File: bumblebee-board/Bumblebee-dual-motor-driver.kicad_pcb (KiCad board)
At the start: 2 copper layers, 91.8 x 75.9 mm, 94 parts, among them J1 ICSP, J10 GND, J11 MOTOR1_A, J12 MOTOR1_B, J13 MOTOR2_A, J14 MOTOR2_B, J15 MAIN+, J16 MAIN-, J17 HEADER, J18 JST-XH, J2 USB_B_Micro, J3 HEADER, J4 HEADER, J5 JST-XH, J6 JST-XH, J7 12V_OUT, J8 5V_OUT, J9 GND, Q1 Q_NMOS_GDS, Q2 Q_NMOS_GDS, Q3 Q_NMOS_GDS, Q4 Q_NMOS_GDS, Q5 Q_NMOS_GDS, Q6 Q_NMOS_GDS, Q7 Q_NMOS_GDS, Q8 Q_NMOS_GDS, SW1 SW_DIP_x04, U1 ATmega328P-AU, U2 FT232RL, U3 74LS08, U4 74LVC2G240, U5 R-78E5.0-0.5, U6 A4940KLPTR-T, U7 A4940KLPTR-T

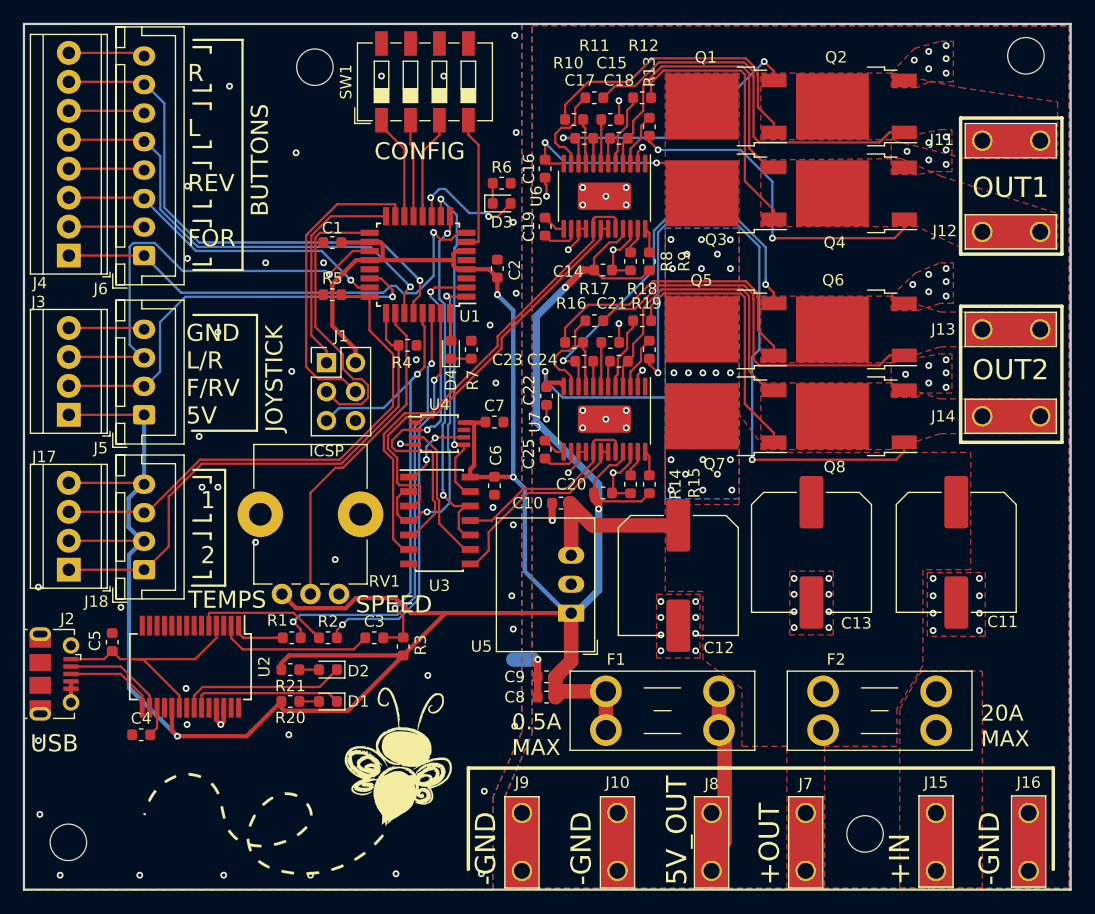
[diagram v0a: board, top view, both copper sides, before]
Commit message: Made bumblebee-compact. Added VT logo to both. Made gerbers. Shipping.
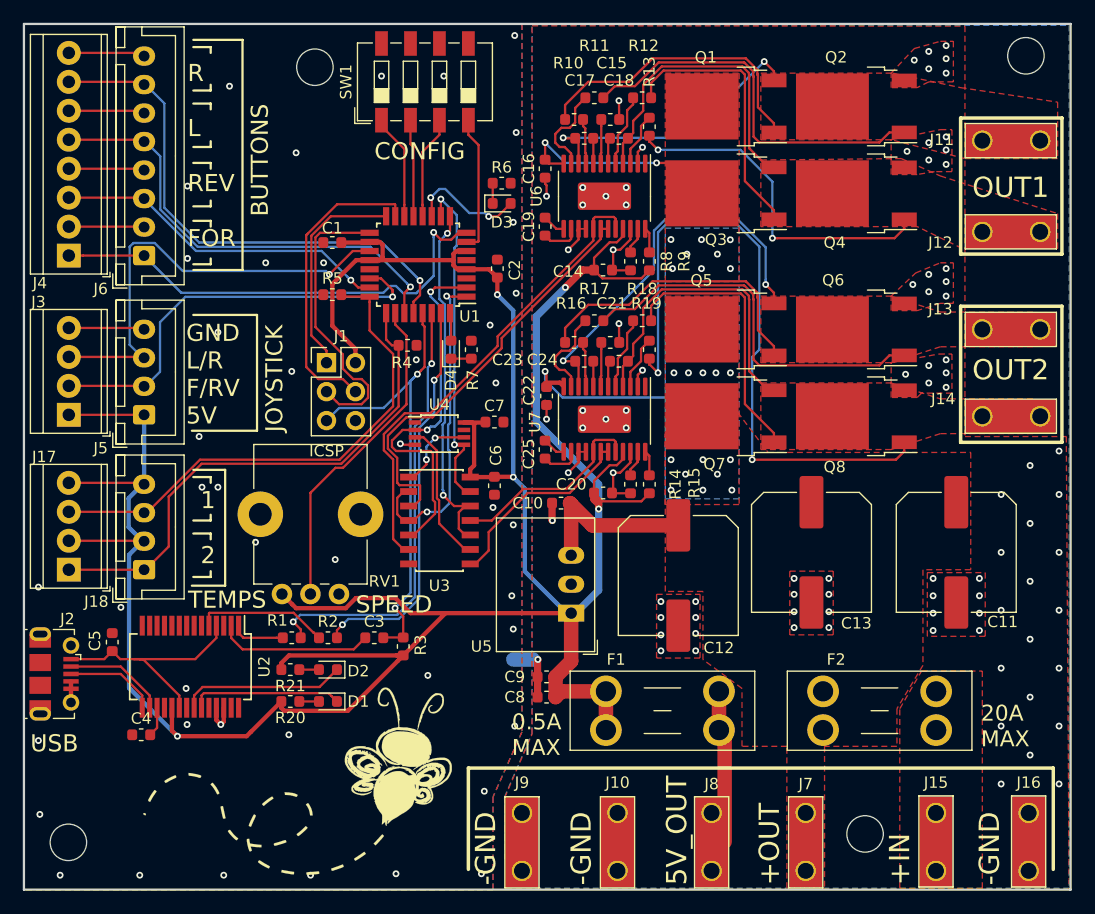
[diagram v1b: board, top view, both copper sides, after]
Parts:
- added G***: LOGO, footprints:vtLogo15mm, B.Cu at (97.0, 86.4)
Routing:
- net GND: vias 113 -> 132
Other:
- board text added: "NOTES: -Fuse type is mini-blade, available at most automotive stores. -Either stripped bare wires can be used on the terminal blocks, or JST XH connectors can be plugged into the white connectors, which are more durable. -The high-current vertical spade terminals are 1/4". -This board is 100% Arduino-compatible, and programmable as an Arduino Uno. Check manual for more information, including pin 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"
- board text removed: "NOTES: -Fuse type is mini-blade, available at most automotive stores. -Either stripped bare wires can be used on the terminal blocks, or JST XH connectors can be plugged in to the white connectors, which are more durable. -This board is 100% Arduino-compatible, and programmable as an Arduino Uno. Check manual for more information, including pin equivalencies and how to control motors. -The high-c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"

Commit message: Bumblebee-board r2 ready to ship.
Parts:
- removed the R13 at (134.2, 87.1)
- removed the R19 at (134.2, 106.7)
- added R14: 27, Resistor_SMD:R_0603_1608Metric, F.Cu at (133.5, 84.6)
- added R15: 27k, Resistor_SMD:R_0603_1608Metric, F.Cu at (134.2, 106.7)
- added R23: 27, Resistor_SMD:R_0603_1608Metric, F.Cu at (132.9, 104.3)
- added R8: 27k, Resistor_SMD:R_0603_1608Metric, F.Cu at (134.2, 87.1)
- moved G*** 16.1 mm to (113.2, 85.7)
- moved U5 5.92 mm to (124.0, 125.0), turned to 270 degrees
- moved R22 1.91 mm to (133.6, 102.2)
- moved R13 1.78 mm to (133.5, 82.8)
- moved R19 1.66 mm to (127.8, 104.3)
- moved J1 1.65 mm to (105.9, 106.2)
- moved R12 1.02 mm to (128.4, 84.6)
- moved C15 0.76 mm to (130.0, 86.5)
- moved R11 0.76 mm to (126.9, 86.5)
- moved C21 0.51 mm to (130.3, 106.0)
- moved R18 0.51 mm to (127.1, 106.0)
- renumbered R9 to R10, R10 to R11, R11 to R12, R12 to R13, R14 to R16, R15 to R17, R16 to R18, R17 to R19, R18 to R22, R8 to R9
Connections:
- U1 pad 1: /MOTOR1_PWM -> /MOTOR2_DIR
- U1 pad 10: /MOTOR2_DIR -> /MOTOR1_PWM
- U5 pad 1: +5V -> VBUS
- U5 pad 3: VBUS -> +5V
- U6 pad 1: (no net) -> /MOTOR1_DRIVER/~RESET
- U7 pad 1: (no net) -> /MOTOR2_DRIVER/~RESET
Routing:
- net VBUS: track 49.8 -> 64.7 mm
- net /MOTOR2_DIR: track 30.0 -> 19.8 mm
- net /MOTOR1_PWM: track 28.2 -> 37.6 mm
- net Net-(Q8-Pad1): track 57.3 -> 52.9 mm
- net Net-(Q4-Pad1): track 30.5 -> 34.8 mm
- net Net-(R22-Pad2): track 6.41 -> 9.26 mm
- net +5V: track 272.4 -> 269.5 mm
- net /MOTOR1_DRIVER/~RESET: track 0.00 -> 2.60 mm
- net /MOTOR2_DRIVER/~RESET: track 0.00 -> 2.60 mm
- net /MOTOR2_B: track 27.3 -> 29.5 mm
- net Net-(Q6-Pad1): track 34.3 -> 36.2 mm
- net Net-(R13-Pad2): track 6.41 -> 8.14 mm
- net Net-(Q7-Pad1): track 23.9 -> 22.3 mm
- net Net-(R23-Pad2): track 4.71 -> 6.25 mm
- net /SCK: track 25.7 -> 24.2 mm
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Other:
- net class Default: trace_width 0.1524 -> 0.2032
- board text added: "5V A1 5V A0"
- board text added: "5V OUT"
- board text added: "9-24V"
- board text added: "Arduino pin numbers this side. Flip for functionality with default firmware."
- board text added: "GND A5 GND A4 GND A0 GND 21"
- board text added: "GND A6 A7 5V"
- board text added: "Hardware files and more info available at https://github.com/willemcvu/ Bumblebee-dual-motor-driver"
- board text added: "NOTES: -Fuse type is mini-blade, available at most automotive stores. -Either stripped bare wires can be used on the terminal blocks, or JST XH connectors can be plugged into the white connectors, which are more durable. -The high-current vertical spade terminals are 1/4". -This board is Arduino-compatible. Check the Github link for more information, including code examples."
- board text added: "Willem Hillier revB 5/27/2019"
- board text removed: "5V_OUT"
- board text removed: "NOTES: -Fuse type is mini-blade, available at most automotive stores. -Either stripped bare wires can be used on the terminal blocks, or JST XH connectors can be plugged into the white connectors, which are more durable. -The high-current vertical spade terminals are 1/4". -This board is 100% Arduino-compatible, and programmable as an Arduino Uno. Check manual for more information, including pin 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"
- board text removed: "Willem Hillier revA 5/9/2019"
